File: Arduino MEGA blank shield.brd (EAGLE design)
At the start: 101.6 x 53.3 mm, 14 parts

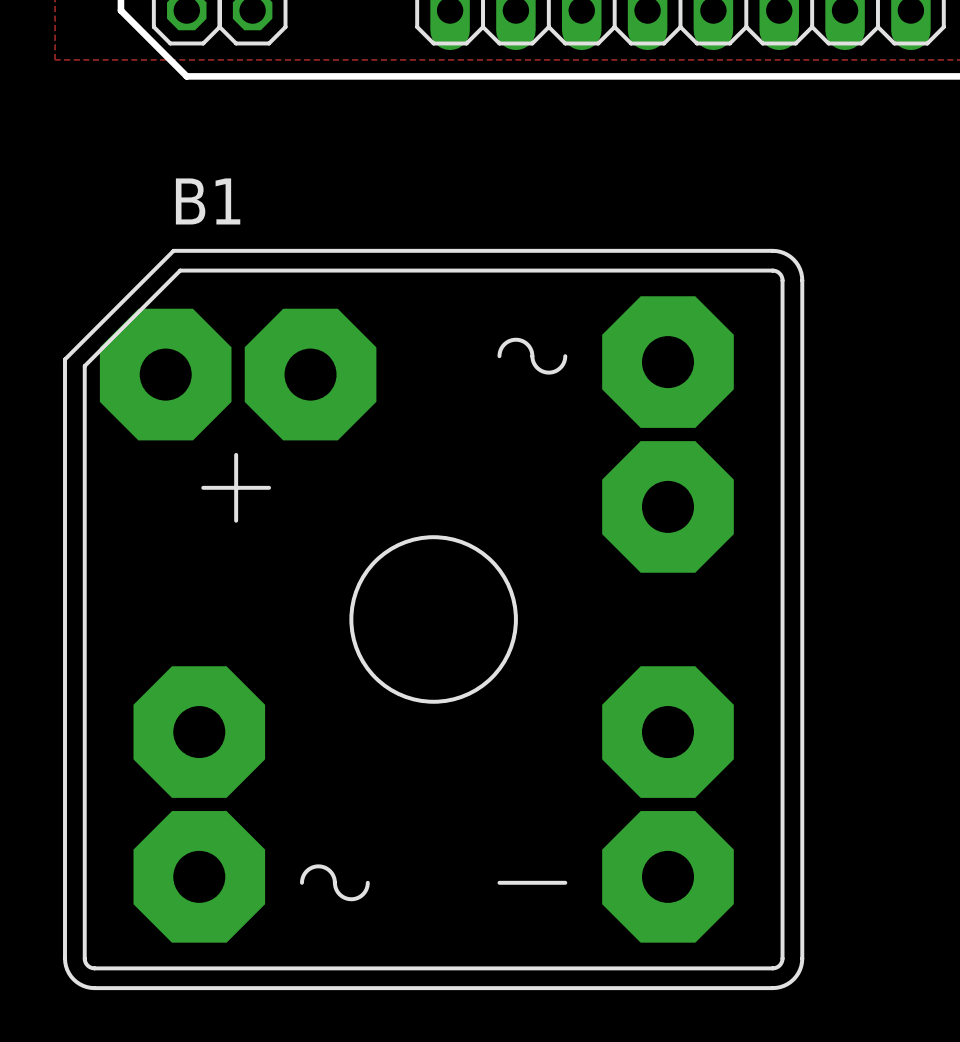
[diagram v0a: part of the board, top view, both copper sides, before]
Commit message: removed dummy part
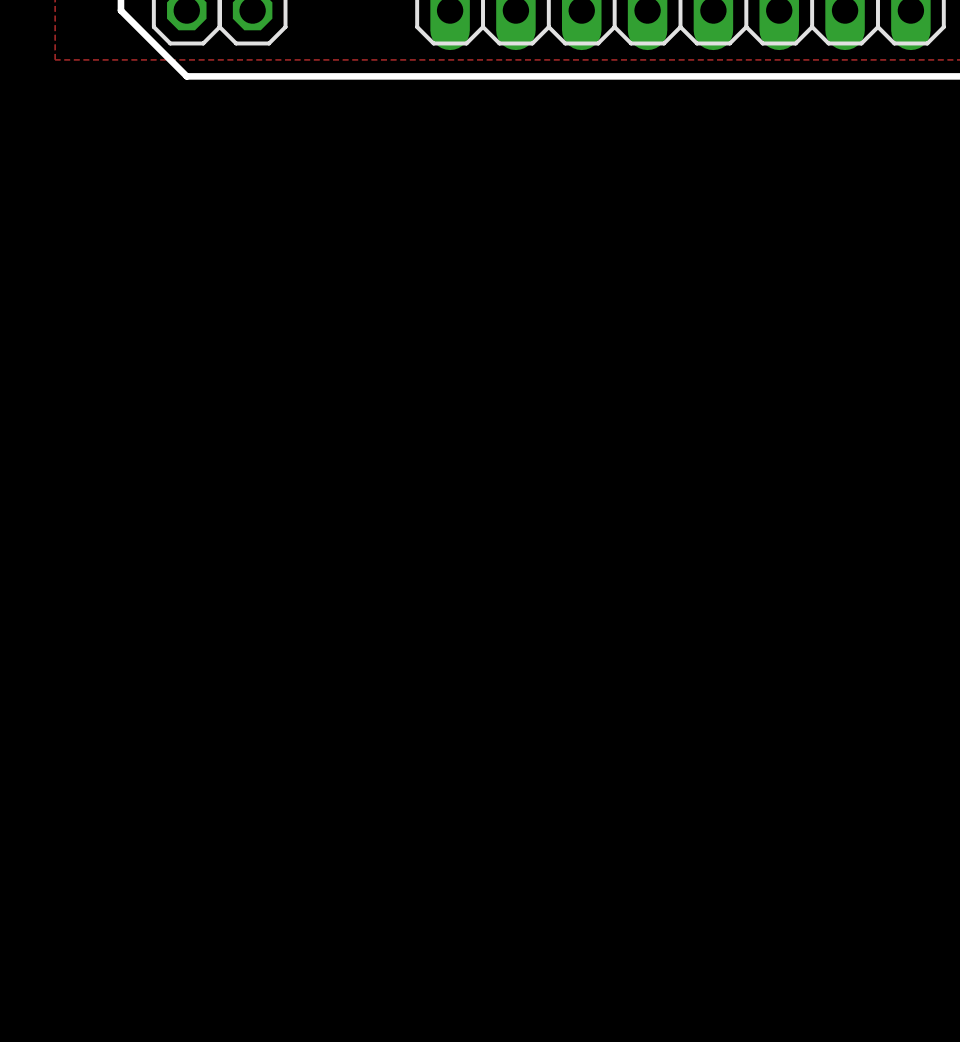
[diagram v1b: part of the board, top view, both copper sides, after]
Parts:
- removed B1: (no value), rectifier:B25A-
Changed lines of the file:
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@@
 <attribute name="VALUE" x="-43.18" y="81.915" size="1.27" layer="27" rot="R180"/>
 </element>
-<element name="B1" library="rectifier" package="B25A-" value="" x="-34.925" y="12.065"/>
 </elements>
 <signals>

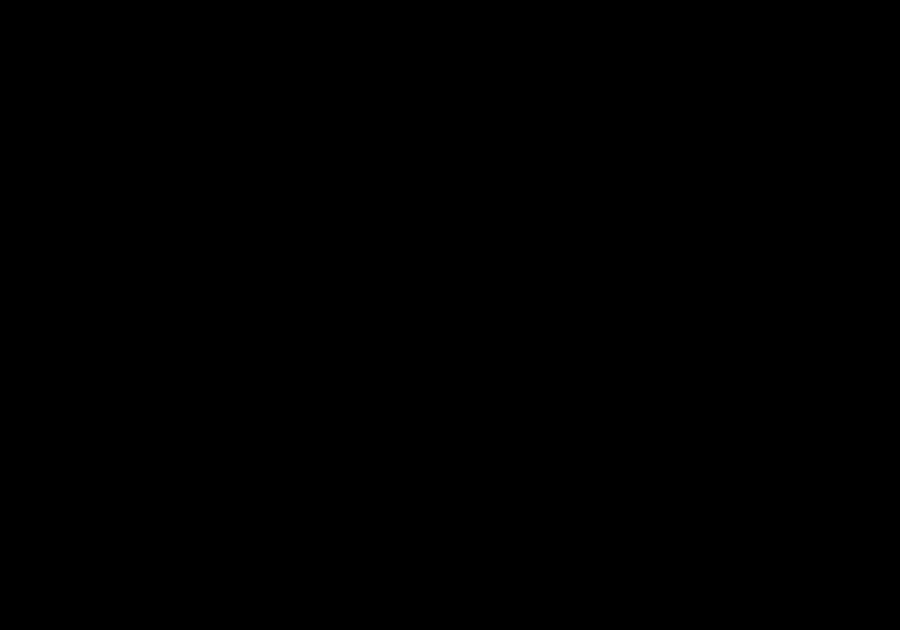
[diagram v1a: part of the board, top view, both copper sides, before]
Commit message: real addition of header
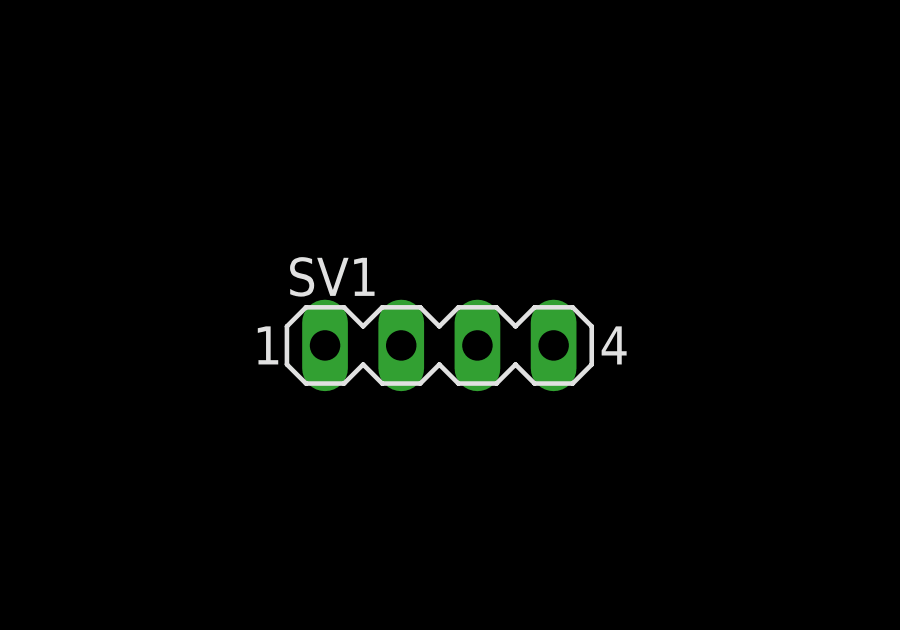
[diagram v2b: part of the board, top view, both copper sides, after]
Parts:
- added SV1: (no value), con-lstb:MA04-1
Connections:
- net PB3: now also SV1.1
- net PL1: now also SV1.2
- net PL3: now also SV1.3
- net PL5: now also SV1.4
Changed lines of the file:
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@@
 <grid distance="25" unitdist="mil" unit="mil" style="lines" multiple="1" display="yes" altdistance="5" altunitdist="mil" altunit="mil"/>
 <layers>
-<layer number="1" name="Top" color="12" fill="1" visible="no" active="yes"/>
+<layer number="1" name="Top" color="12" fill="1" visible="yes" active="yes"/>
 <layer number="2" name="Route2" color="1" fill="3" visible="no" active="no"/>
 <layer number="3" name="Route3" color="4" fill="3" visible="no" active="no"/>
@@
 <layer number="14" name="Route14" color="1" fill="6" visible="no" active="no"/>
 <layer number="15" name="Route15" color="4" fill="6" visible="no" active="no"/>
-<layer number="16" name="Bottom" color="9" fill="1" visible="no" active="yes"/>
+<layer number="16" name="Bottom" color="9" fill="1" visible="yes" active="yes"/>
 <layer number="17" name="Pads" color="2" fill="1" visible="yes" active="yes"/>
 <layer number="18" name="Vias" color="14" fill="1" visible="no" active="yes"/>
 <layer number="19" name="Unrouted" color="13" fill="1" visible="no" active="yes"/>
 <layer number="20" name="Dimension" color="3" fill="1" visible="yes" active="yes"/>
-<layer number="21" name="tPlace" color="7" fill="1" visible="no" active="yes"/>
-<layer number="22" name="bPlace" color="7" fill="1" visible="no" active="yes"/>
-<layer number="23" name="tOrigins" color="15" fill="1" visible="no" active="yes"/>
-<layer number="24" name="bOrigins" color="15" fill="1" visible="no" active="yes"/>
-<layer number="25" name="tNames" color="7" fill="1" visible="no" active="yes"/>
-<layer number="26" name="bNames" color="11" fill="1" visible="no" active="yes"/>
-<layer number="27" name="tValues" color="12" fill="1" visible="no" active="yes"/>
-<layer number="28" name="bValues" color="7" fill="1" visible="no" active="yes"/>
+<layer number="21" name="tPlace" color="7" fill="1" visible="yes" active="yes"/>
+<layer number="22" name="bPlace" color="7" fill="1" visible="yes" active="yes"/>
+<layer number="23" name="tOrigins" color="15" fill="1" visible="yes" active="yes"/>
+<layer number="24" name="bOrigins" color="15" fill="1" visible="yes" active="yes"/>
+<layer number="25" name="tNames" color="7" fill="1" visible="yes" active="yes"/>
+<layer number="26" name="bNames" color="11" fill="1" visible="yes" active="yes"/>
+<layer number="27" name="tValues" color="12" fill="1" visible="yes" active="yes"/>
+<layer number="28" name="bValues" color="7" fill="1" visible="yes" active="yes"/>
 <layer number="29" name="tStop" color="7" fill="3" visible="no" active="yes"/>
 <layer number="30" name="bStop" color="7" fill="6" visible="no" active="yes"/>
@@
 <layer number="42" name="bRestrict" color="1" fill="10" visible="no" active="yes"/>
 <layer number="43" name="vRestrict" color="2" fill="10" visible="no" active="yes"/>
-<layer number="44" name="Drills" color="7" fill="1" visible="no" active="yes"/>
-<layer number="45" name="Holes" color="7" fill="1" visible="no" active="yes"/>
+<layer number="44" name="Drills" color="7" fill="1" visible="yes" active="yes"/>
+<layer number="45" name="Holes" color="7" fill="1" visible="yes" active="yes"/>
 <layer number="46" name="Milling" color="3" fill="1" visible="no" active="yes"/>
-<layer number="47" name="Measures" color="7" fill="1" visible="no" active="yes"/>
+<layer number="47" name="Measures" color="7" fill="1" visible="yes" active="yes"/>
 <layer number="48" name="Document" color="7" fill="1" visible="no" active="yes"/>
 <layer number="49" name="Reference" color="13" fill="1" visible="no" active="yes"/>
@@
 <attribute name="VALUE" x="-43.18" y="81.915" size="1.27" layer="27" rot="R180"/>
 </element>
+<element name="SV1" library="con-lstb" package="MA04-1" value="" x="5.715" y="65.405">
+<attribute name="OC_NEWARK" value="unknown" x="5.715" y="65.405" size="1.778" layer="27" display="off"/>
+<attribute name="MPN" value="" x="5.715" y="65.405" size="1.778" layer="27" display="off"/>
+<attribute name="MF" value="" x="5.715" y="65.405" size="1.778" layer="27" display="off"/>
+<attribute name="OC_FARNELL" value="unknown" x="5.715" y="65.405" size="1.778" layer="27" display="off"/>
+</element>
 </elements>
 <signals>
@@
 <signal name="PB3">
 <contactref element="JP2" pad="4"/>
+<contactref element="SV1" pad="1"/>
+<wire x1="-41.91" y1="73.66" x2="1.905" y2="65.405" width="0" layer="19" extent="1-1"/>
 </signal>
 <signal name="PB2">
@@
 <signal name="PL1">
 <contactref element="JP2" pad="6"/>
+<contactref element="SV1" pad="2"/>
+<wire x1="-41.91" y1="71.12" x2="4.445" y2="65.405" width="0" layer="19" extent="1-1"/>
 </signal>
 <signal name="PL2">
@@
 <signal name="PL3">
 <contactref element="JP2" pad="8"/>
+<contactref element="SV1" pad="3"/>
+<wire x1="-41.91" y1="68.58" x2="6.985" y2="65.405" width="0" layer="19" extent="1-1"/>
 </signal>
 <signal name="PL4">
@@
 <signal name="PL5">
 <contactref element="JP2" pad="10"/>
+<contactref element="SV1" pad="4"/>
+<wire x1="-41.91" y1="66.04" x2="9.525" y2="65.405" width="0" layer="19" extent="1-1"/>
 </signal>
 <signal name="PL6">

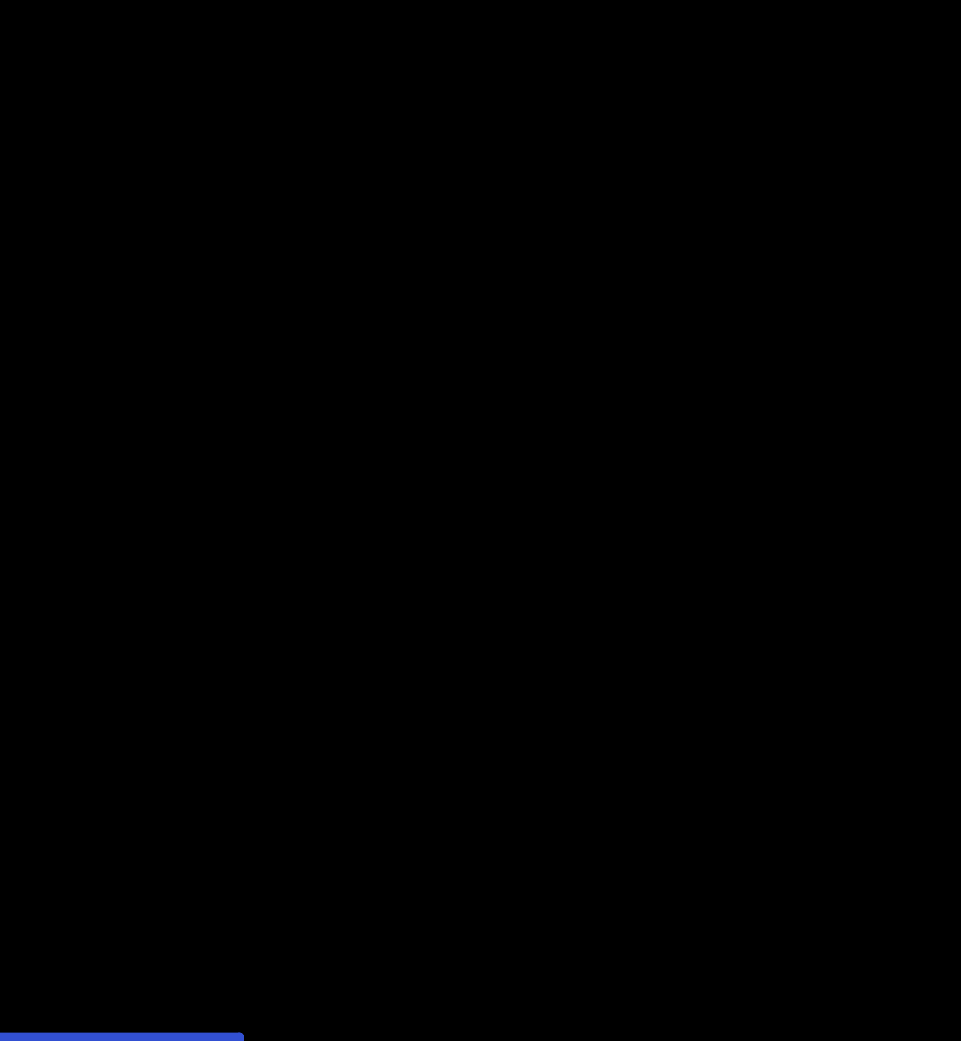
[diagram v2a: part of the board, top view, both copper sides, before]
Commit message: added motor controls
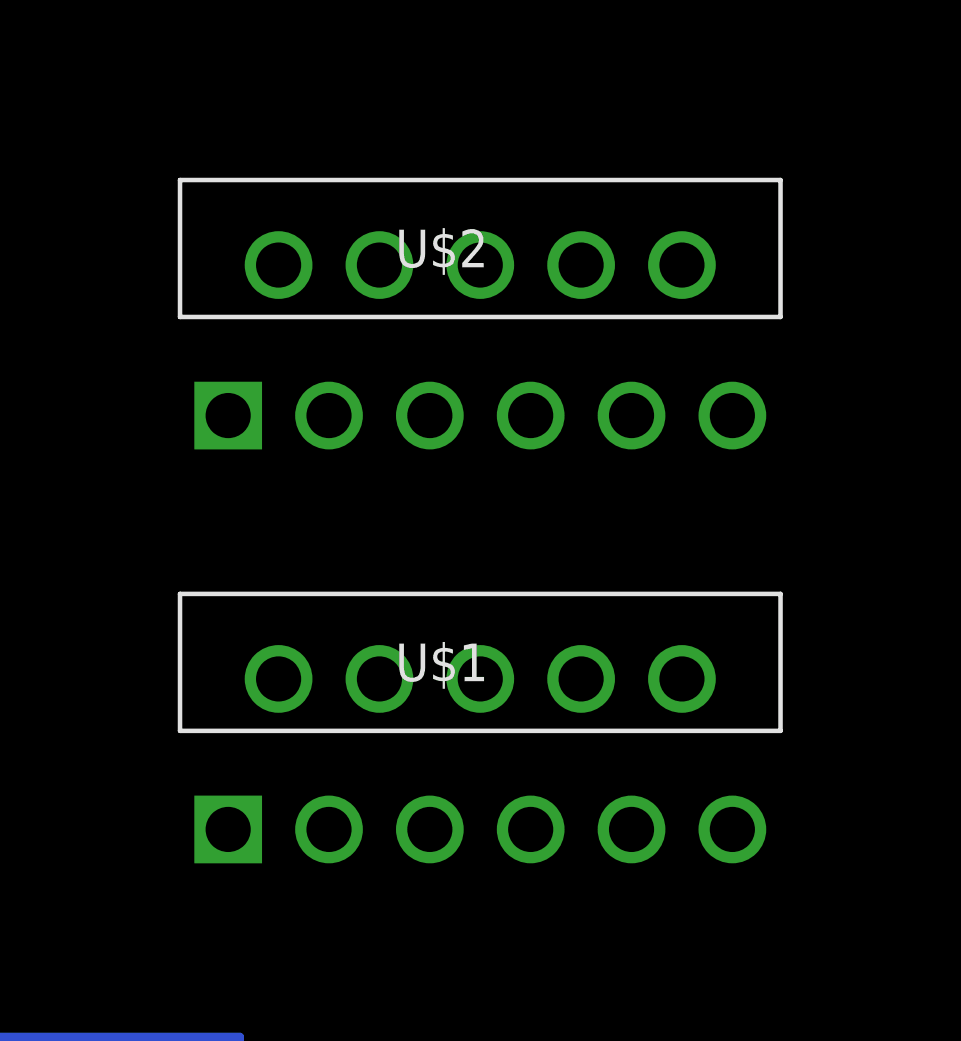
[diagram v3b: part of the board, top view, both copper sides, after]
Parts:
- added U$1, U$2: LMD18200_NDJ_11, mega2560shield:TA11B
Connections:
- new net VS: U$1.6, U$2.6
- net GND: now also U$1.7, U$2.7
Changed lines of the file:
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@@
 <attribute name="OC_FARNELL" value="unknown" x="5.715" y="65.405" size="1.778" layer="27" display="off"/>
+</element>
+<element name="U$1" library="mega2560shield" package="TA11B" value="LMD18200_NDJ_11" x="37.465" y="64.135">
+<attribute name="VENDOR" value="National" x="37.465" y="64.135" size="1.778" layer="27" display="off"/>
+<attribute name="MANUFACTURER_PART_NUMBER" value="lmd18200tnopb" x="37.465" y="64.135" size="1.778" layer="27" display="off"/>
+</element>
+<element name="U$2" library="mega2560shield" package="TA11B" value="LMD18200_NDJ_11" x="37.465" y="78.105">
+<attribute name="VENDOR" value="National" x="37.465" y="78.105" size="1.778" layer="27" display="off"/>
+<attribute name="MANUFACTURER_PART_NUMBER" value="lmd18200tnopb" x="37.465" y="78.105" size="1.778" layer="27" display="off"/>
 </element>
 </elements>
@@
 <vertex x="51.435" y="85.725"/>
 </polygon>
+<contactref element="U$1" pad="7"/>
+<contactref element="U$2" pad="7"/>
+<wire x1="30.6578" y1="52.8574" x2="25.4" y2="35.56" width="0" layer="19" extent="1-1"/>
+<wire x1="30.6578" y1="66.8274" x2="30.6578" y2="52.8574" width="0" layer="19" extent="1-1"/>
 </signal>
 <signal name="AREF">
@@
 <contactref element="PWMH" pad="6"/>
 </signal>
+<signal name="VS">
+<contactref element="U$1" pad="6"/>
+<contactref element="U$2" pad="6"/>
+<wire x1="28.956" y1="57.9374" x2="28.956" y2="71.9074" width="0" layer="19" extent="1-1"/>
+</signal>
 </signals>
